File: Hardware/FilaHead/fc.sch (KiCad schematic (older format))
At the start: 3 parts, among them J0 Conn_2, SW1 PowerSel

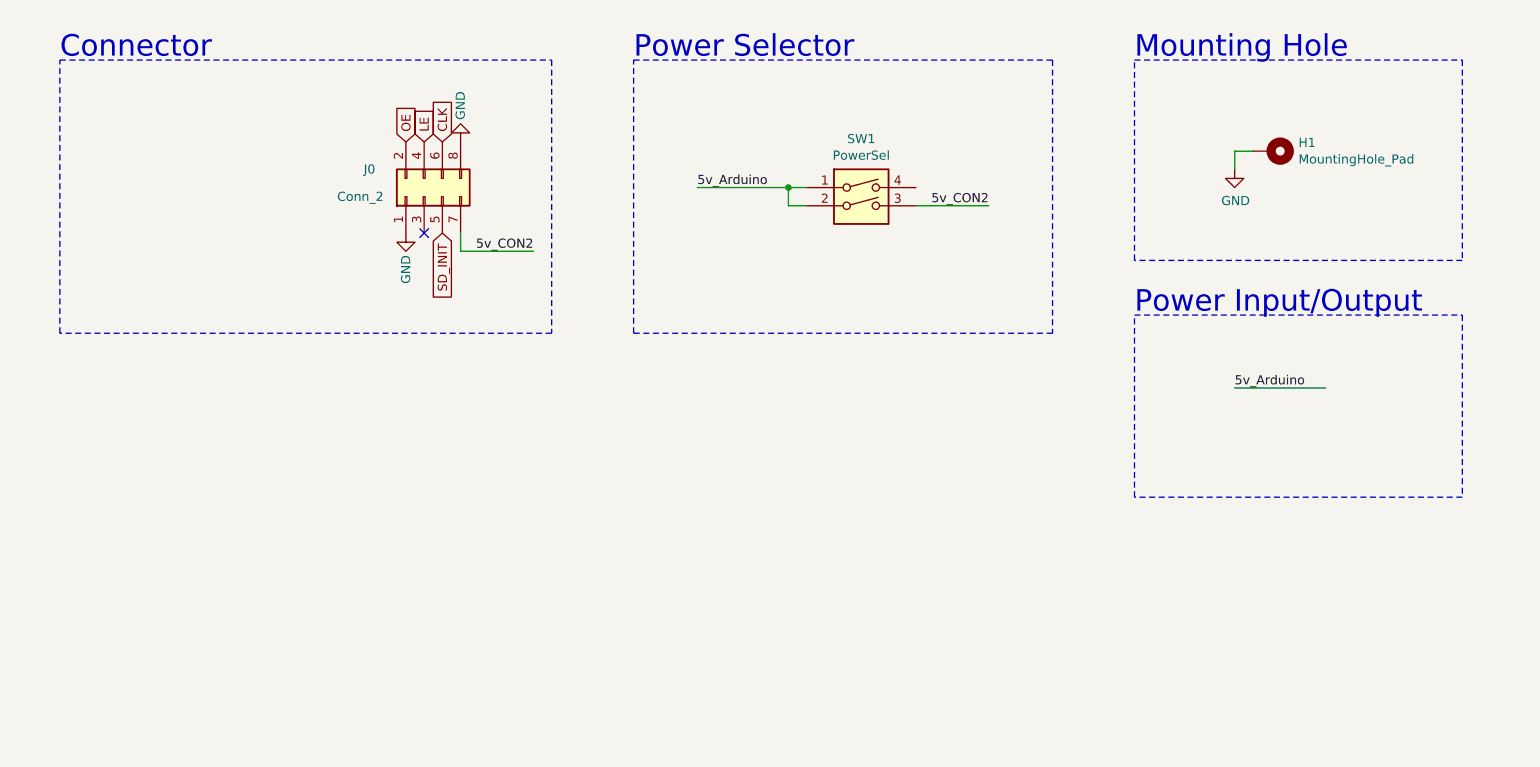
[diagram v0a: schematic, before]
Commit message: updated arduino nano connector
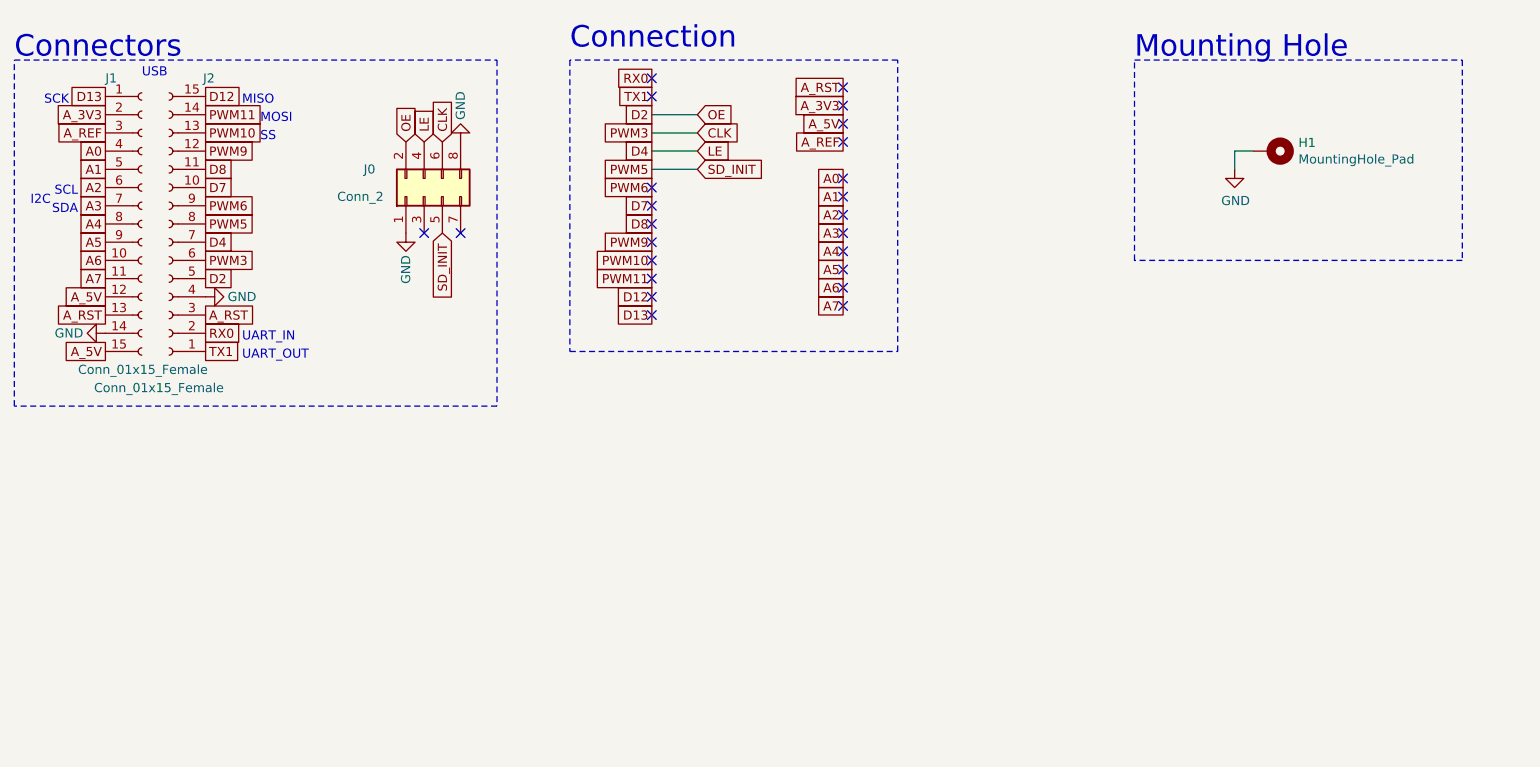
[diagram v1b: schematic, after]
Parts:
- removed SW1: PowerSel, Button_Switch_SMD:SW_DIP_SPSTx02_Slide_KingTek_DSHP02TS_W7.62mm_P1.27mm, symbol Switch:SW_DIP_x02
- added J1, J2: Conn_01x15_Female, symbol Connector:Conn_01x15_Female
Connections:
- net labels added: A0, A1, A2, A3, A4, A5, A6, A7, A_3V3, A_5V, A_REF, A_RST, D12, D13, D2, D4, D7, D8, PWM10, PWM11, PWM3, PWM5, PWM6, PWM9, RX0, TX1
- net labels removed: 5v_Arduino, 5v_CON2
- wire segments 10 -> 6
- no-connect marks 1 -> 24
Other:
- note added: "Connection"
- note added: "Connectors"
- note added: "I2C"
- note added: "MISO"
- note added: "MOSI"
- note added: "SCK"
- note added: "SCL"
- note added: "SDA"
- note added: "SS"
- note added: "UART_IN"
- note added: "UART_OUT"
- note added: "USB"
- note removed: "Connector"
- note removed: "Power Input/Output"
- note removed: "Power Selector"

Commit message: updated hardware and RPi codes
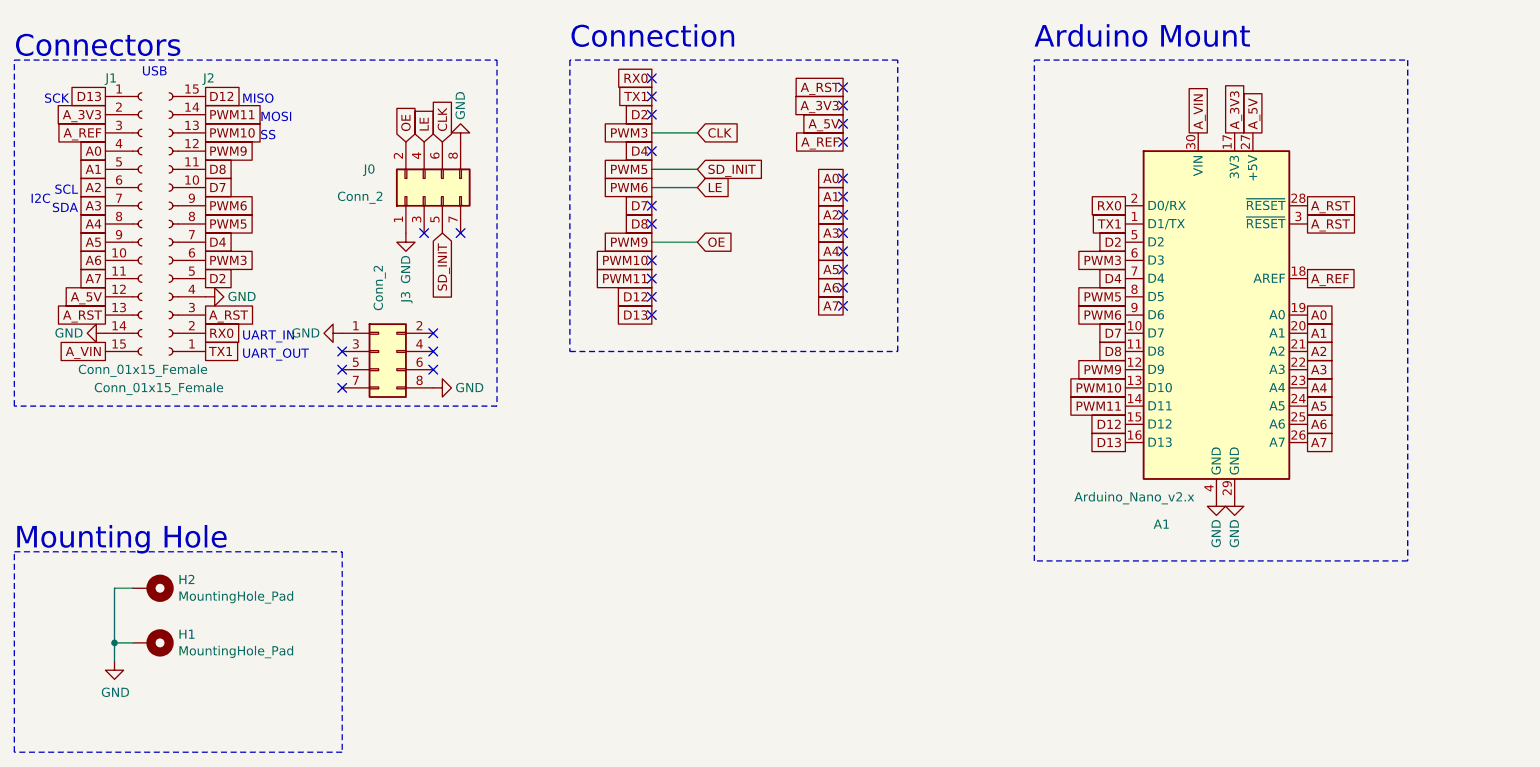
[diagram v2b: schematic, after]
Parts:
- added A1: Arduino_Nano_v2.x, Module:Arduino_Nano, symbol MCU_Module:Arduino_Nano_v2.x
- added H2: MountingHole_Pad, MountingHole:MountingHole_3.2mm_M3_Pad_Via, symbol Mechanical:MountingHole_Pad
- added J3: Conn_2, Connector_PinSocket_2.54mm:PinSocket_2x04_P2.54mm_Vertical, symbol Connector_Generic:Conn_02x04_Odd_Even
- J1, J2: footprint (none) -> Connector_PinHeader_2.54mm:PinHeader_1x15_P2.54mm_Vertical
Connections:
- net A0: now also A1.19 (A0)
- net A1: now also A1.20 (A1)
- net A2: now also A1.21 (A2)
- net A3: now also A1.22 (A3)
- net A4: now also A1.23 (A4)
- net A5: now also A1.24 (A5)
- net A6: now also A1.25 (A6)
- net A7: now also A1.26 (A7)
- net A_3V3: now also A1.17 (3V3)
- net A_5V: now also A1.27 (+5V); no longer J1.15 (Pin_15)
- net A_REF: now also A1.18 (AREF)
- net A_RST: now also A1.28 (~RESET), A1.3 (~RESET)
- net CLK: now also A1.6 (D3)
- net D12: now also A1.15 (D12)
- net D13: now also A1.16 (D13)
- net D2: now also A1.5 (D2); no longer J0.2 (Pin_2)
- net D4: now also A1.7 (D4); no longer J0.4 (Pin_4)
- net D7: now also A1.10 (D7)
- net D8: now also A1.11 (D8)
- net GND: now also A1.29 (GND), A1.4 (GND), H2.1, J3.1 (Pin_1), J3.8 (Pin_8)
- net PWM10: now also A1.13 (D10)
- net PWM11: now also A1.14 (D11)
- net PWM5: now also A1.8 (D5)
- net RX0: now also A1.2 (D0/RX)
- net TX1: now also A1.1 (D1/TX)
- net PWM6 renamed LE
- net LE: now also J0.4 (Pin_4), A1.9 (D6)
- net PWM9 renamed OE
- net OE: now also J0.2 (Pin_2), A1.12 (D9)
- new net A_VIN: A1.30 (VIN), J1.15 (Pin_15)
- no-connect marks 24 -> 30
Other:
- note added: "Arduino Mount"
- moved on the sheet: H1

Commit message: Updated Fila Head
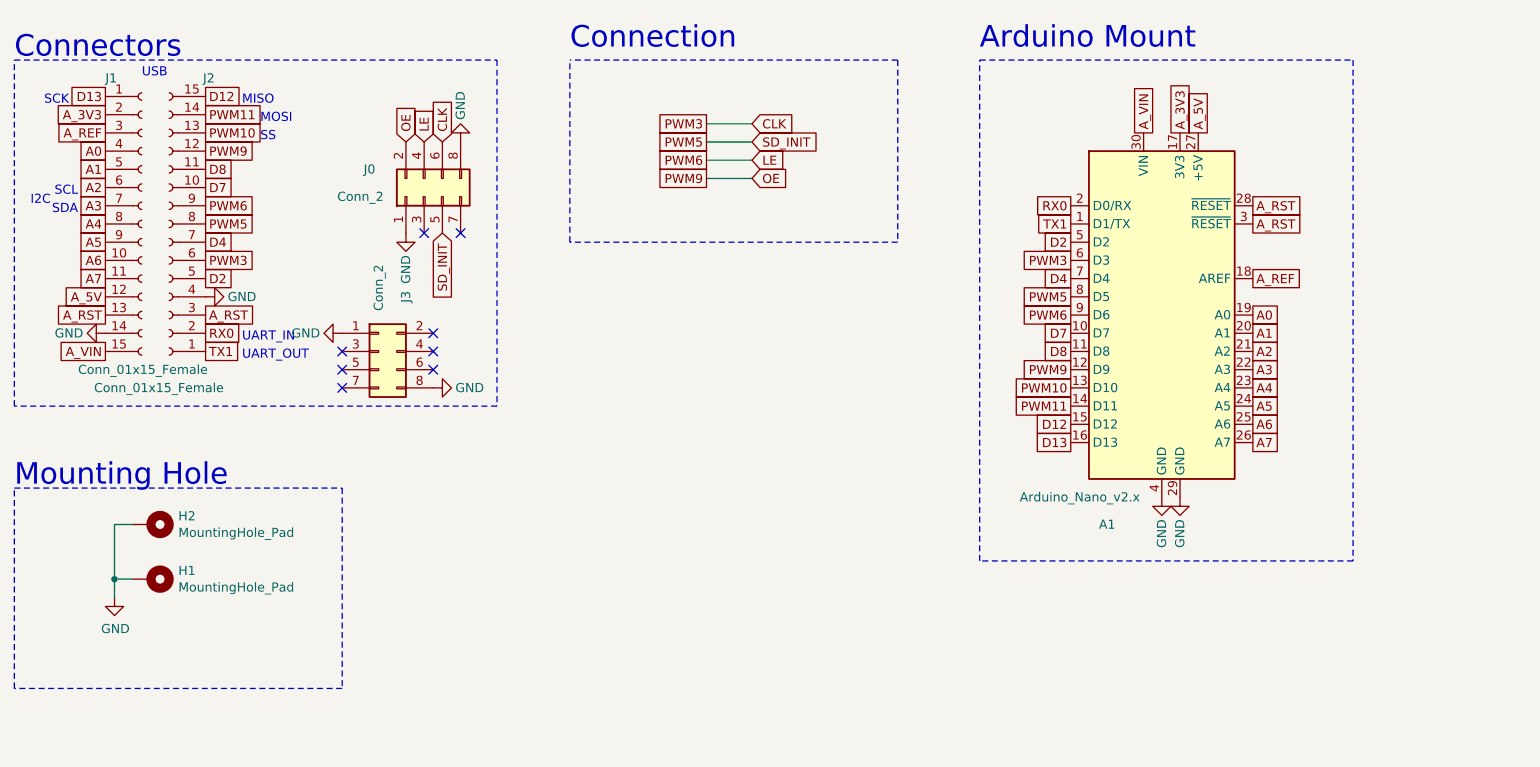
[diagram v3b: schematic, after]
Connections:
- no-connect marks 30 -> 8
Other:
- moved on the sheet: A1, H1, H2

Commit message: updated packages
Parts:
- J0, J3: footprint Connector_PinSocket_2.54mm:PinSocket_2x04_P2.54mm_Vertical -> Connector_PinHeader_2.54mm:PinHeader_2x04_P2.54mm_Vertical
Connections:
- net CLK: now also J0.5 (Pin_5); no longer J0.6 (Pin_6)
- net GND: now also J0.2 (Pin_2), J0.7 (Pin_7), J3.2 (Pin_2), J3.7 (Pin_7); no longer J0.1 (Pin_1), J0.8 (Pin_8), J3.1 (Pin_1), J3.8 (Pin_8)
- net LE: now also J0.3 (Pin_3); no longer J0.4 (Pin_4)
- net OE: now also J0.1 (Pin_1); no longer J0.2 (Pin_2)
- net PWM5: now also J0.6 (Pin_6); no longer J0.5 (Pin_5)
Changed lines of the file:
@@
 F 0 "J0" V 4150 2700 50  0000 C CNN
 F 1 "Conn_2" V 4000 2750 50  0000 C CNN
-F 2 "Connector_PinSocket_2.54mm:PinSocket_2x04_P2.54mm_Vertical" H 4000 2400 50  0001 C CNN
+F 2 "Connector_PinHeader_2.54mm:PinHeader_2x04_P2.54mm_Vertical" H 4000 2400 50  0001 C CNN
 F 3 "~" H 4000 2400 50  0001 C CNN
 	1    4000 2400
 	0    -1   -1   0
 $EndComp
+Text GLabel 4100 2100 1    50   Input ~ 0
+SD_INIT
 Text GLabel 4100 2600 3    50   Input ~ 0
-SD_INIT
-Text GLabel 4100 2100 1    50   Input ~ 0
 CLK
-Text GLabel 4000 2100 1    50   Input ~ 0
+Text GLabel 4000 2600 3    50   Input ~ 0
 LE
-Text GLabel 3900 2100 1    50   Input ~ 0
+Text GLabel 3900 2600 3    50   Input ~ 0
 OE
 $Comp
 L power:GND #PWR0101
 U 1 1 6069982E
-P 3900 2600
-F 0 "#PWR0101" H 3900 2350 50  0001 C CNN
-F 1 "GND" V 3900 2400 50  0000 C CNN
-F 2 "" H 3900 2600 50  0001 C CNN
-F 3 "" H 3900 2600 50  0001 C CNN
-	1    3900 2600
-	1    0    0    -1
+P 3900 2100
+F 0 "#PWR0101" H 3900 1850 50  0001 C CNN
+F 1 "GND" V 3900 1900 50  0000 C CNN
+F 2 "" H 3900 2100 50  0001 C CNN
+F 3 "" H 3900 2100 50  0001 C CNN
+	1    3900 2100
+	1    0    0    1
 $EndComp
 $Comp
 L power:GND #PWR0104
 U 1 1 6067A66E
-P 4200 2100
-F 0 "#PWR0104" H 4200 1850 50  0001 C CNN
-F 1 "GND" V 4200 1900 50  0000 C CNN
-F 2 "" H 4200 2100 50  0001 C CNN
-F 3 "" H 4200 2100 50  0001 C CNN
-	1    4200 2100
-	-1   0    0    1
+P 4200 2600
+F 0 "#PWR0104" H 4200 2350 50  0001 C CNN
+F 1 "GND" V 4200 2400 50  0000 C CNN
+F 2 "" H 4200 2600 50  0001 C CNN
+F 3 "" H 4200 2600 50  0001 C CNN
+	1    4200 2600
+	-1   0    0    -1
 $EndComp
 Text Notes 1750 1650 0    118  ~ 0
@@
 Text Notes 1750 4000 0    118  ~ 0
 Mounting Hole
-NoConn ~ 4000 2600
-NoConn ~ 4200 2600
 $Comp
 L Connector:Conn_01x15_Female J1
@@
 F 0 "J3" V 3900 3550 50  0000 C CNN
 F 1 "Conn_2" V 3750 3600 50  0000 C CNN
-F 2 "Connector_PinSocket_2.54mm:PinSocket_2x04_P2.54mm_Vertical" H 3750 3250 50  0001 C CNN
+F 2 "Connector_PinHeader_2.54mm:PinHeader_2x04_P2.54mm_Vertical" H 3750 3250 50  0001 C CNN
 F 3 "~" H 3750 3250 50  0001 C CNN
 	1    3750 3250
@@
 L power:GND #PWR0108
 U 1 1 606CE8DB
-P 3550 3150
-F 0 "#PWR0108" H 3550 2900 50  0001 C CNN
-F 1 "GND" V 3550 2950 50  0000 C CNN
-F 2 "" H 3550 3150 50  0001 C CNN
-F 3 "" H 3550 3150 50  0001 C CNN
-	1    3550 3150
-	0    1    1    0
+P 4050 3150
+F 0 "#PWR0108" H 4050 2900 50  0001 C CNN
+F 1 "GND" V 4050 2950 50  0000 C CNN
+F 2 "" H 4050 3150 50  0001 C CNN
+F 3 "" H 4050 3150 50  0001 C CNN
+	1    4050 3150
+	0    -1   1    0
 $EndComp
 $Comp
 L power:GND #PWR0109
 U 1 1 606CEFB1
-P 4050 3450
-F 0 "#PWR0109" H 4050 3200 50  0001 C CNN
-F 1 "GND" V 4050 3250 50  0000 C CNN
-F 2 "" H 4050 3450 50  0001 C CNN
-F 3 "" H 4050 3450 50  0001 C CNN
-	1    4050 3450
-	0    -1   -1   0
-$EndComp
-NoConn ~ 3550 3450
+P 3550 3450
+F 0 "#PWR0109" H 3550 3200 50  0001 C CNN
+F 1 "GND" V 3550 3250 50  0000 C CNN
+F 2 "" H 3550 3450 50  0001 C CNN
+F 3 "" H 3550 3450 50  0001 C CNN
+	1    3550 3450
+	0    1    -1   0
+$EndComp
 NoConn ~ 3550 3350
 NoConn ~ 3550 3250
-NoConn ~ 4050 3150
 NoConn ~ 4050 3250
 NoConn ~ 4050 3350
@@
 Wire Notes Line
 	4800 2650 4800 1650
+NoConn ~ 4050 3450
+NoConn ~ 3550 3150
+NoConn ~ 4000 2100
+NoConn ~ 4200 2100
 $EndSCHEMATC
